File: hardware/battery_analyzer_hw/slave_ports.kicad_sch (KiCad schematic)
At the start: 9 parts, among them J4 CH0, J5 CH1, J6 CH2, J7 CH3

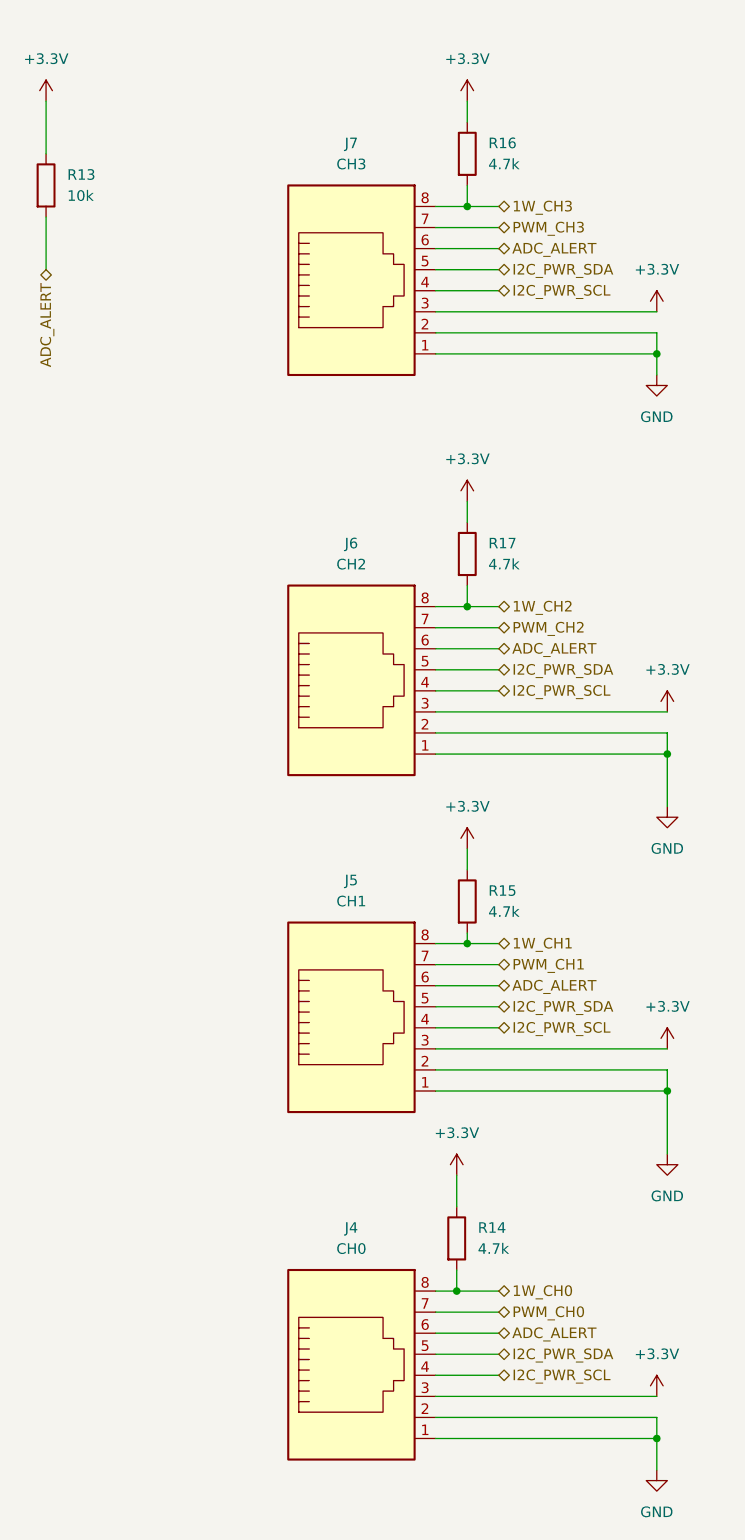
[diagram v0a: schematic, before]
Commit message: refactor(hw): upgrade RJ45 to shielded, repurpose pin 1 for fan PWM fix(hw): optimize RJ45 pinout for T568B twisted pairs
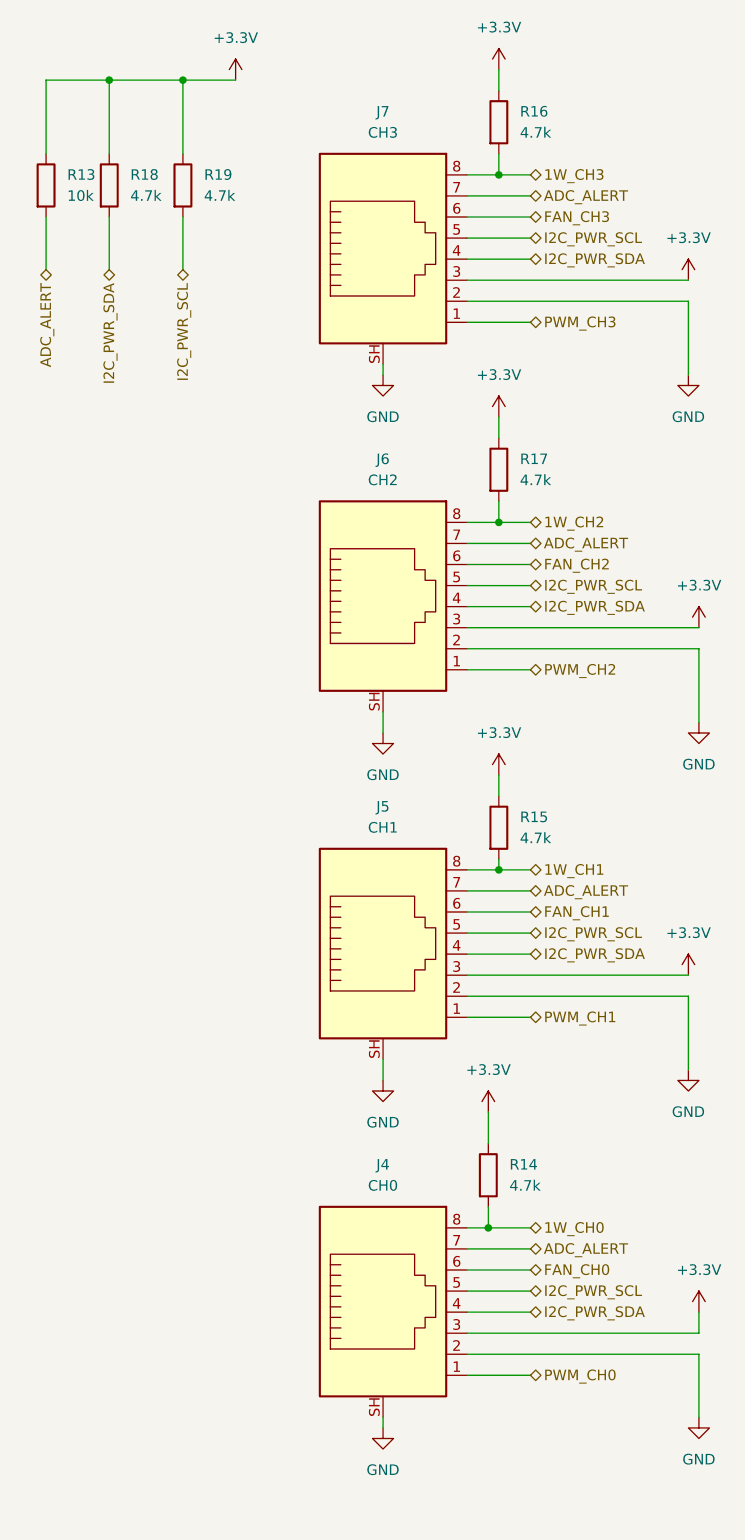
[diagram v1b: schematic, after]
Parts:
- added R18, R19: 4.7k, symbol Device:R
- J4, J5, J6, J7: symbol Connector:RJ45 -> Connector:RJ45_Shielded
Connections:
- net +3.3V: now also R18.1, R19.1
- net ADC_ALERT: now also J4.7, J5.7, J6.7, J7.7; no longer J4.6, J5.6, J6.6, J7.6
- net GND: now also J4.SH, J5.SH, J6.SH, J7.SH; no longer J4.1, J5.1, J6.1, J7.1
- net I2C_PWR_SCL: now also J4.5, J5.5, J6.5, J7.5, R19.2; no longer J4.4, J5.4, J6.4, J7.4
- net I2C_PWR_SDA: now also J4.4, J5.4, J6.4, J7.4, R18.2; no longer J4.5, J5.5, J6.5, J7.5
- net PWM_CH0: now also J4.1; no longer J4.7
- net PWM_CH1: now also J5.1; no longer J5.7
- net PWM_CH2: now also J6.1; no longer J6.7
- net PWM_CH3: now also J7.1; no longer J7.7
- new net FAN_CH0: J4.6
- new net FAN_CH1: J5.6
- new net FAN_CH2: J6.6
- new net FAN_CH3: J7.6
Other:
- moved on the sheet: R14, R15, R16, R17

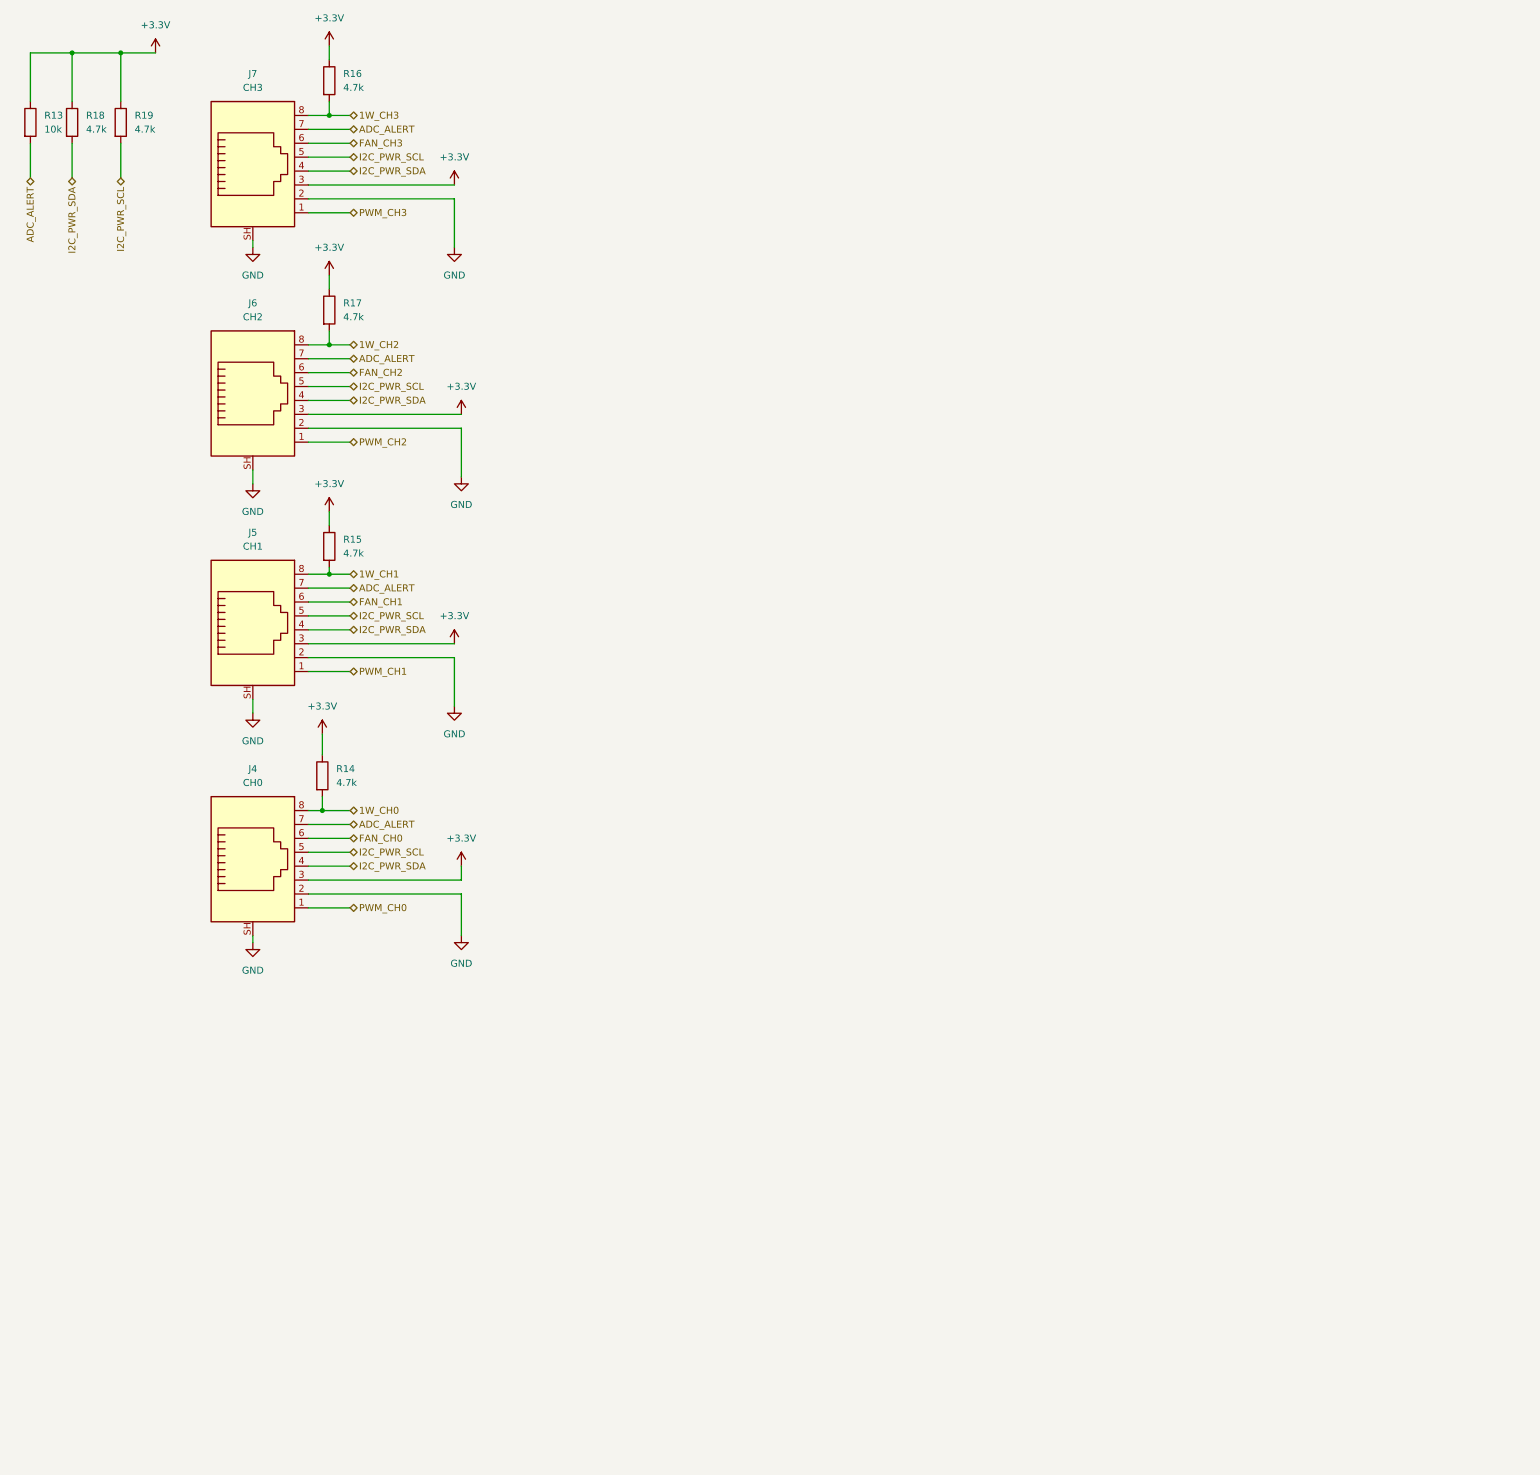
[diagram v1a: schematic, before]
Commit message: feat(hw): add Master-board RJ45 protection circuit with PTC and BAT54S clamps
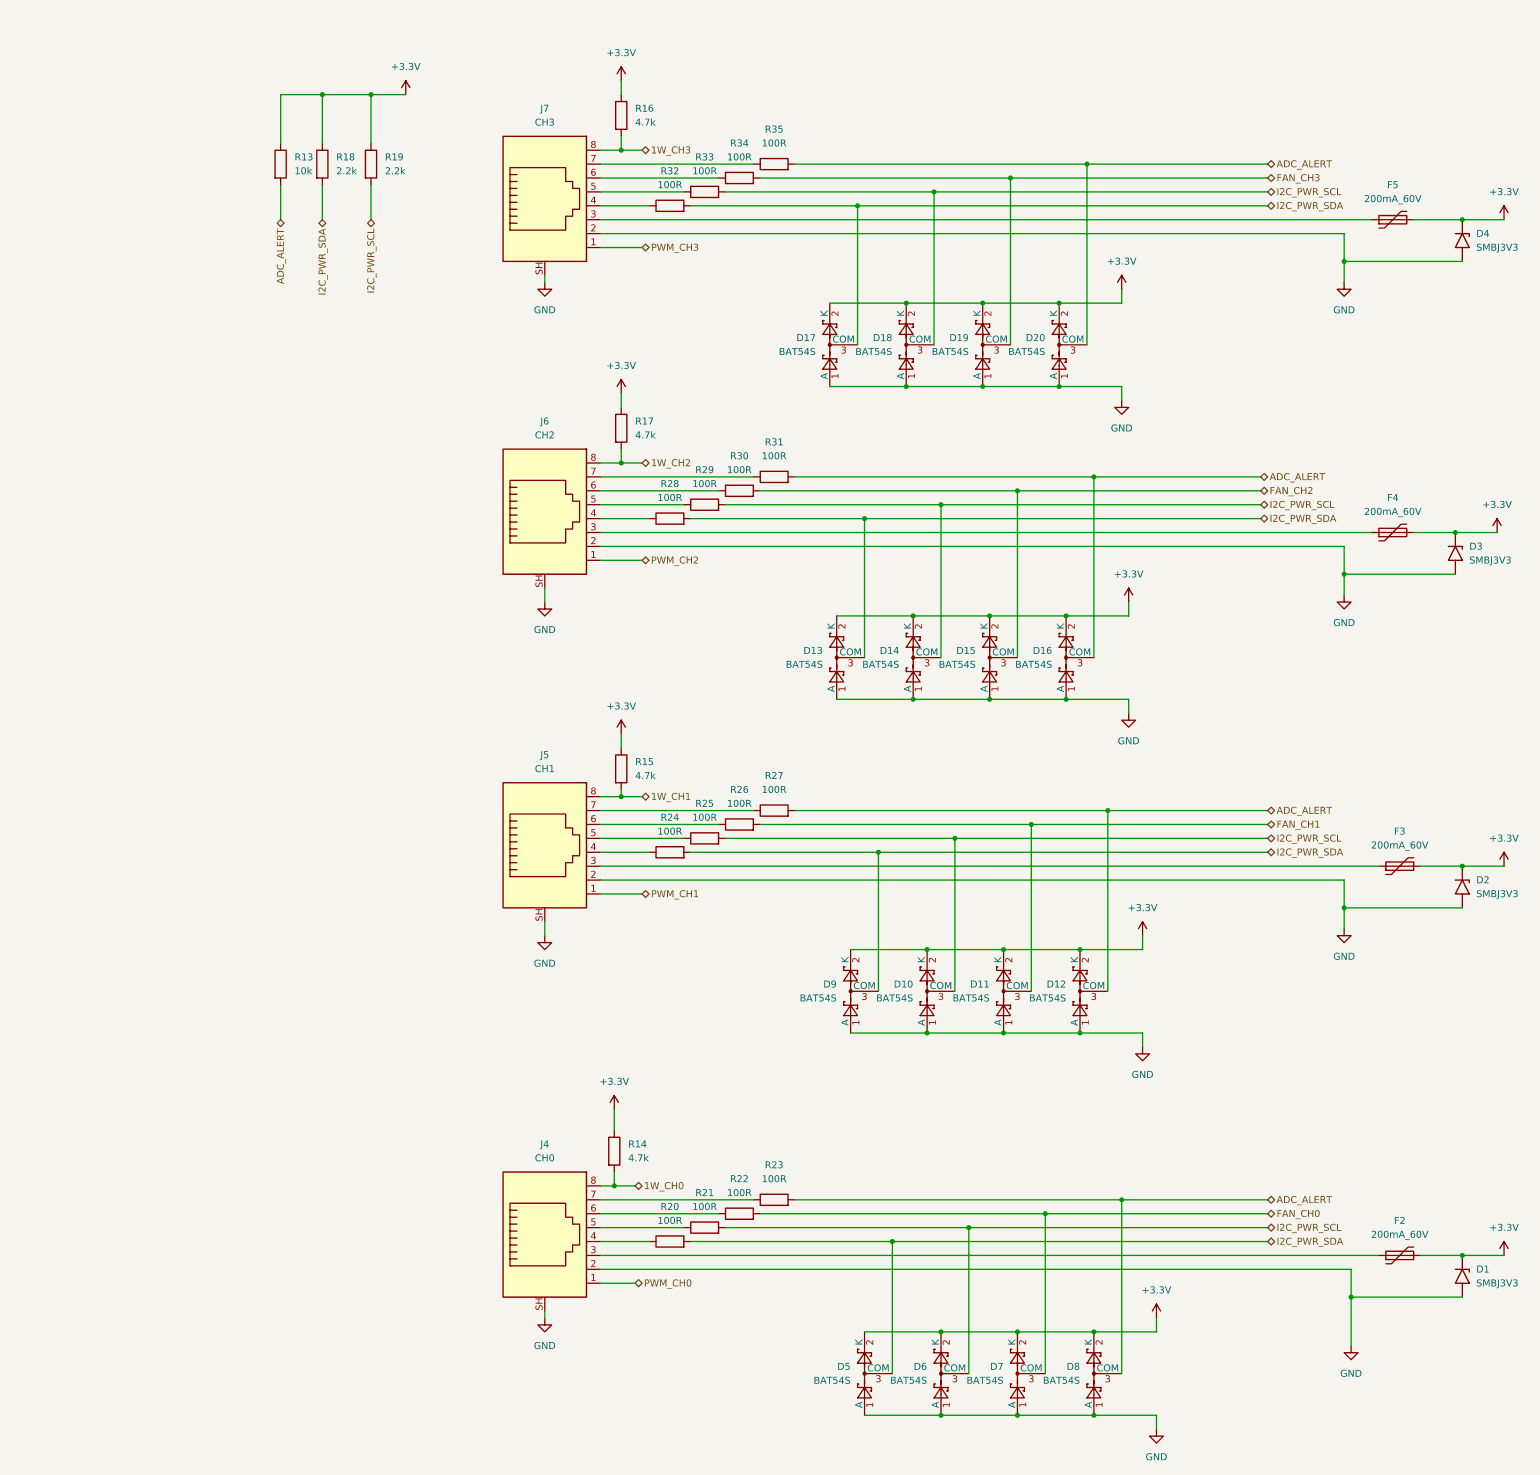
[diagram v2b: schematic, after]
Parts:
- added D1, D2, D3, D4: SMBJ3V3, Diode_SMD:D_SMB_Handsoldering, symbol Diode:SMF10A
- added D10, D11, D12, D13, D14, D15, D16, D17, D18, D19, D20, D5, D6, D7, D8, D9: BAT54S, Package_TO_SOT_SMD:SOT-23, symbol Diode:BAT54S
- added F2, F3, F4, F5: 200mA_60V, Fuse:Fuse_1206_3216Metric, symbol Device:Polyfuse
- added R20, R21, R22, R23, R24, R25, R26, R27, R28, R29, R30, R31, R32, R33, R34, R35: 100R, Resistor_SMD:R_0805_2012Metric_Pad1.20x1.40mm_HandSolder, symbol Device:R
- R13: footprint (none) -> Resistor_SMD:R_0805_2012Metric_Pad1.20x1.40mm_HandSolder
- R18, R19: value 4.7k -> 2.2k; footprint (none) -> Resistor_SMD:R_0805_2012Metric_Pad1.20x1.40mm_HandSolder
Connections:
- net +3.3V: now also D1.1 (A1), D10.2 (K), D11.2 (K), D12.2 (K), D13.2 (K), D14.2 (K), D15.2 (K), D16.2 (K), D17.2 (K), D18.2 (K), D19.2 (K), D2.1 (A1), D20.2 (K), D3.1 (A1), D4.1 (A1), D5.2 (K), D6.2 (K), D7.2 (K), D8.2 (K), D9.2 (K), F2.2, F3.2, F4.2, F5.2; no longer J4.3, J5.3, J6.3, J7.3
- net ADC_ALERT: now also D12.3 (COM), D16.3 (COM), D20.3 (COM), D8.3 (COM), R23.2, R27.2, R31.2, R35.2; no longer J4.7, J5.7, J6.7, J7.7
- net FAN_CH0: now also D7.3 (COM), R22.2; no longer J4.6
- net FAN_CH1: now also D11.3 (COM), R26.2; no longer J5.6
- net FAN_CH2: now also D15.3 (COM), R30.2; no longer J6.6
- net FAN_CH3: now also D19.3 (COM), R34.2; no longer J7.6
- net GND: now also D1.2 (A2), D10.1 (A), D11.1 (A), D12.1 (A), D13.1 (A), D14.1 (A), D15.1 (A), D16.1 (A), D17.1 (A), D18.1 (A), D19.1 (A), D2.2 (A2), D20.1 (A), D3.2 (A2), D4.2 (A2), D5.1 (A), D6.1 (A), D7.1 (A), D8.1 (A), D9.1 (A)
- net I2C_PWR_SCL: now also D10.3 (COM), D14.3 (COM), D18.3 (COM), D6.3 (COM), R21.2, R25.2, R29.2, R33.2; no longer J4.5, J5.5, J6.5, J7.5
- net I2C_PWR_SDA: now also D13.3 (COM), D17.3 (COM), D5.3 (COM), D9.3 (COM), R20.2, R24.2, R28.2, R32.2; no longer J4.4, J5.4, J6.4, J7.4
- new net: F5.1, J7.3
- new net: J7.4, R32.1
- new net: J7.5, R33.1
- new net: J7.6, R34.1
- new net: J7.7, R35.1
- new net: J6.4, R28.1
- new net: J6.5, R29.1
- new net: F2.1, J4.3
- new net: J6.6, R30.1
- new net: F3.1, J5.3
- new net: J5.4, R24.1
- new net: J5.5, R25.1
- new net: J5.6, R26.1
- new net: J5.7, R27.1
- new net: J4.6, R22.1
- new net: J4.7, R23.1
- new net: J4.5, R21.1
- new net: J4.4, R20.1
- new net: F4.1, J6.3
- new net: J6.7, R31.1
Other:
- moved on the sheet: J4, J5, J6, J7, R13, R14, R15, R16, R17, R18, R19
